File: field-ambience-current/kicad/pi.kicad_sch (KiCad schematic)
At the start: 9 parts, among them J4 SWD 1.27mm (SWCLK/GND/SWDIO), SW11 Reset 6mm SMD, SW12 BOOTSEL 6mm SMD (DNP for THT-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, U1 Raspberry_Pi_Pico2 (RP2350)

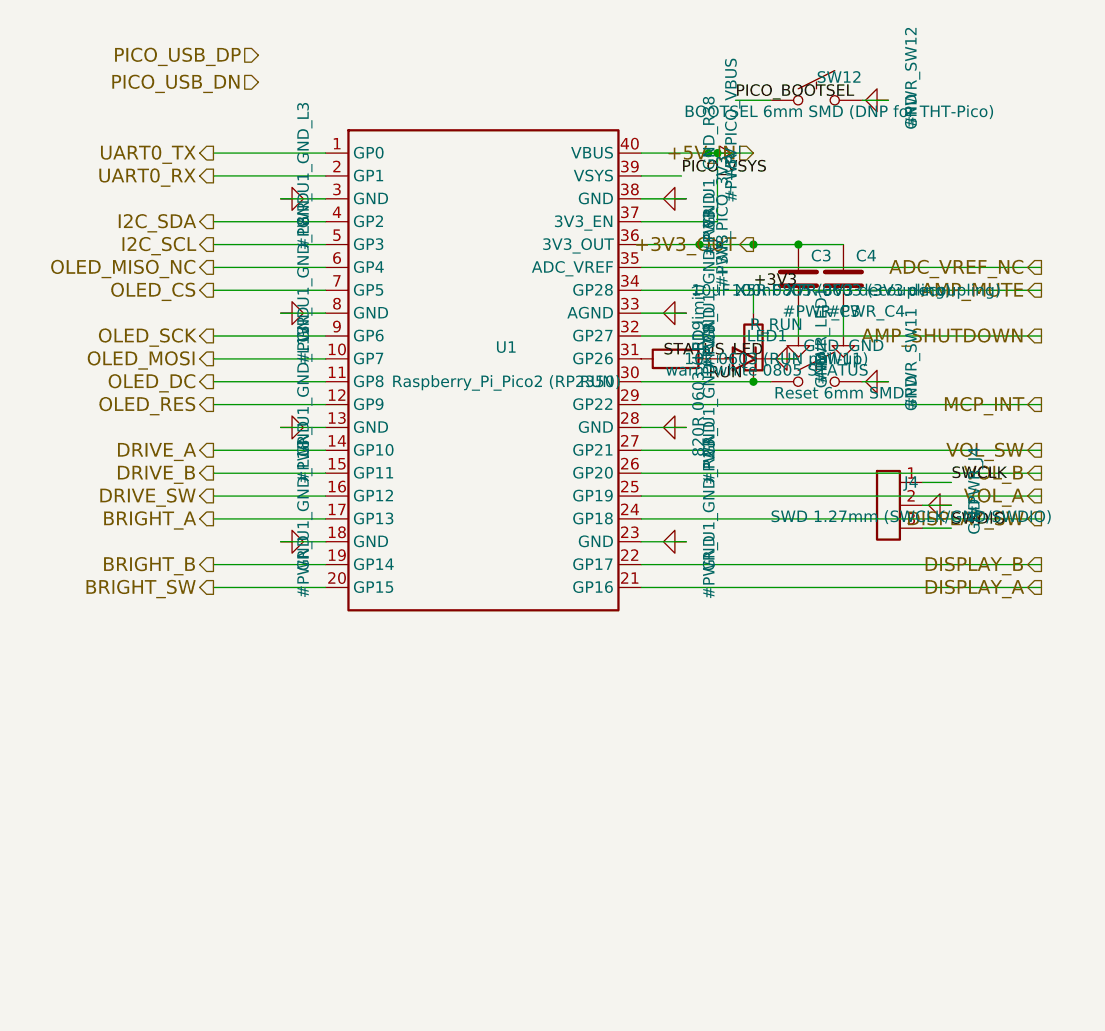
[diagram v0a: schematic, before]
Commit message: Add Sheet 7 (Pi Zero 2 W GPIO Header) per SPEC v0.6 §1/§8
J2 2x20 GPIO Header für Pi Zero 2 W:
- Pin 2, 4: +5V Power-Injection (von unserer PCB-Rail zum Pi)
- Pin 6, 9, 14, 20, 25, 30, 34, 39: GND (8x Pi GND-Pins)
- Pin 1, 17: NC (Pi 3V3 output ungenutzt — unsere 3V3 kommt vom Pico SMPS)

UART (115200) Pi ↔ Pico:
- Pin 10 (Pi GPIO15 RX) ← UART0_TX (von Pico GP0 direkt)
- Pin 8 (Pi GPIO14 TX) → R1 1k series → UART0_RX (zu Pico GP1, per SPEC v0.6 §5 BOM)

I²S Audio Pi → PCM5102A:
- Pin 12 (Pi GPIO18 PCM_CLK) → I2S_BCK
- Pin 35 (Pi GPIO19 PCM_FS) → I2S_LRCK
- Pin 40 (Pi GPIO21 PCM_DOUT) → I2S_DOUT

Alle 23 ungenutzten GPIOs (3, 5, 7, 11, 13, 15, 16, 18, 19, 21-24, 26-29,
31-33, 36-38) als NC-Labels mit informativen Namen markiert
(NC_GPIO2_SDA1, NC_GPIO10_MOSI, etc).

Root sheet: Pi-Sheet bei (330, 40) size (60, 130) mit 5 sheet-pins.
Pico-Sheet bekommt UART0_TX (output) + UART0_RX (input) auf linker Seite.
Label-bridges für UART (Pico↔Pi) und I2S (Pi→Audio).

Conn_02x20 generic lib_symbol generator hinzugefügt (alternating
odd/even Pin-Numbering, 2.54mm spacing).

Analyzer: 0 functional errors (3 VM-001 false positives unverändert).
19 warnings (von 24 gefallen, UART/I2S jetzt closed loop). 83 components
total (28 caps, 24 resistors, 16 switches, 6 connectors, 4 ICs, 2 diodes,
1 fuse, 1 ferrite, 1 LED).

J2 pin_nets verifiziert: alle Power-Pins korrekt, alle GND-Pins korrekt,
UART/I2S-Verbindungen passen zum SPEC §8.

**Damit ist die KiCad-Schematic-Eingabe für SPEC v0.6 komplett.**
Next Steps: ERC clean in KiCad GUI, PCB-Layout, DRC, BOM, JLC-Order.
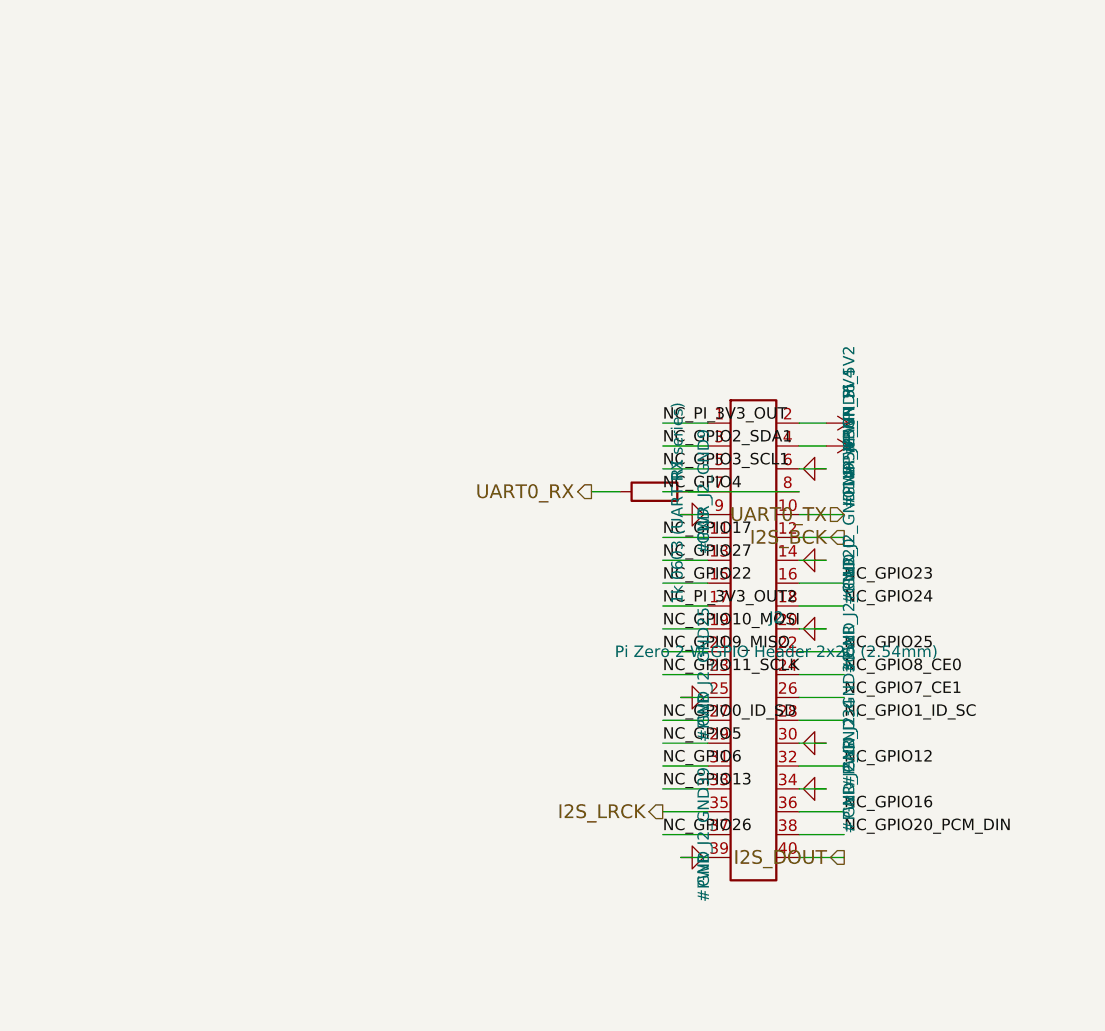
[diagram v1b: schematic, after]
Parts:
- removed C3: 10uF X5R 0805 (3V3 decoupling), Capacitor_SMD:C_0805_2012Metric, symbol Device:C
- removed C4: 100nF X7R 0603 (3V3 decoupling), Capacitor_SMD:C_0603_1608Metric, symbol Device:C
- removed J4: SWD 1.27mm (SWCLK/GND/SWDIO), Connector_PinHeader_1.27mm:PinHeader_1x03_P1.27mm_Vertical, symbol Connector:Conn_01x03
- removed LED1: warm white 0805 STATUS, LED_SMD:LED_0805_2012Metric, symbol Device:LED
- removed R19: 820R 0603 (LED limit), Resistor_SMD:R_0603_1608Metric, symbol Device:R
- removed R_RUN: 10k 0603 (RUN pull-up), Resistor_SMD:R_0603_1608Metric, symbol Device:R
- removed SW11: Reset 6mm SMD, Button_Switch_SMD:SW_SPST_TL3342, symbol Switch:SW_Push
- removed SW12: BOOTSEL 6mm SMD (DNP for THT-Pico), Button_Switch_SMD:SW_SPST_TL3342, symbol Switch:SW_Push
- removed U1: Raspberry_Pi_Pico2 (RP2350), MCU_Module:RPi_Pico_SMD_TH, symbol MCU:Pico2
- added J2: Pi Zero 2 W GPIO Header 2x20 (2.54mm), Connector_PinHeader_2.54mm:PinHeader_2x20_P2.54mm_Vertical, symbol Connector:Conn_02x20
- added R1: 1k 0603 (UART RX series), Resistor_SMD:R_0603_1608Metric, symbol Device:R
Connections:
- net +5V: now also J2.2 (Pin_2), J2.4 (Pin_4)
- net GND: now also J2.14 (Pin_14), J2.20 (Pin_20), J2.25 (Pin_25), J2.30 (Pin_30), J2.34 (Pin_34), J2.39 (Pin_39), J2.6 (Pin_6), J2.9 (Pin_9)
- net UART0_RX: now also R1.1
- net UART0_TX: now also J2.10 (Pin_10)
- new net I2S_BCK: J2.12 (Pin_12)
- new net I2S_DOUT: J2.40 (Pin_40)
- new net I2S_LRCK: J2.35 (Pin_35)
- new net NC_GPIO0_ID_SD: J2.27 (Pin_27)
- new net NC_GPIO10_MOSI: J2.19 (Pin_19)
- new net NC_GPIO11_SCLK: J2.23 (Pin_23)
- new net NC_GPIO12: J2.32 (Pin_32)
- new net NC_GPIO13: J2.33 (Pin_33)
- new net NC_GPIO16: J2.36 (Pin_36)
- new net NC_GPIO17: J2.11 (Pin_11)
- new net NC_GPIO1_ID_SC: J2.28 (Pin_28)
- new net NC_GPIO20_PCM_DIN: J2.38 (Pin_38)
- new net NC_GPIO22: J2.15 (Pin_15)
- new net NC_GPIO23: J2.16 (Pin_16)
- new net NC_GPIO24: J2.18 (Pin_18)
- new net NC_GPIO25: J2.22 (Pin_22)
- new net NC_GPIO26: J2.37 (Pin_37)
- new net NC_GPIO27: J2.13 (Pin_13)
- new net NC_GPIO2_SDA1: J2.3 (Pin_3)
- new net NC_GPIO3_SCL1: J2.5 (Pin_5)
- new net NC_GPIO4: J2.7 (Pin_7), J2.8 (Pin_8), R1.2
- new net NC_GPIO5: J2.29 (Pin_29)
- new net NC_GPIO6: J2.31 (Pin_31)
- new net NC_GPIO7_CE1: J2.26 (Pin_26)
- new net NC_GPIO8_CE0: J2.24 (Pin_24)
- new net NC_GPIO9_MISO: J2.21 (Pin_21)
- new net NC_PI_3V3_OUT: J2.1 (Pin_1)
- new net NC_PI_3V3_OUT2: J2.17 (Pin_17)
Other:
- title: Field Ambience PCB — Sheet 2: Pico 2 (RP2350) -> Field Ambience PCB — Sheet 7: Pi Zero 2 W GPIO Header

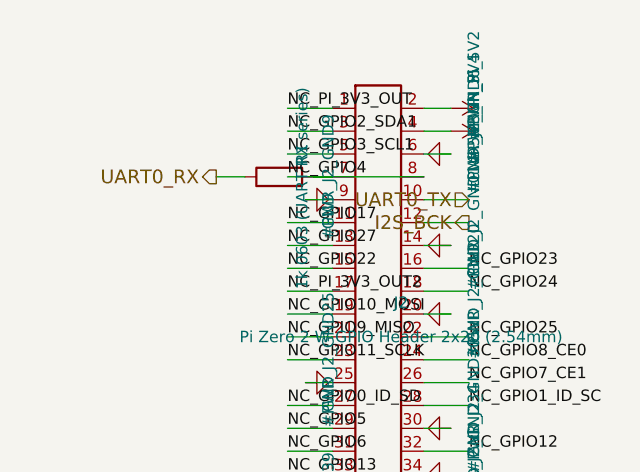
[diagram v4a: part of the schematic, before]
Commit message: v0.6.3-r2: PAM8403 SHDN/MUTE pull-downs + UART naming + TODO list
Addresses 2nd-iteration ChatGPT review findings (most that don't need
KiCad GUI). All TODO items documented in PCB_TODO.md.

B4: PAM8403H /SHDN and /MUTE hardware pull-downs
- R_MUTE_PD 10k from pin 5 (/MUTE) to GND
- R_SHDN_PD 10k from pin 12 (/SHDN) to GND
- Default state during Pico boot/reset = both LOW = Amp OFF + MUTED
- Pico firmware drives HIGH only after power-sequencing per SPEC §5
- Prevents undefined Amp state during boot transients (pop/click safety)

I7: UART net naming disambiguated
- Old: UART0_TX / UART0_RX (perspective-ambiguous)
- New:
  - PICO_TX_PI_RX (Pico GP0 → Pi GPIO15 pin 10)
  - PI_TX_PICO_RX (Pi GPIO14 pin 8 → R1 1k → Pico GP1)
- Changed in pico_sheet, pi_sheet, root_sheet (pins + labels)

N4: Titleblock revs synced
- audio.kicad_sch: v0.6.1 → v0.6.3
- power_tree.kicad_sch: v0.6 → v0.6.3
- Comments updated to reflect current state

N5: Stale comments cleanup
- power_tree_sheet: USB-C pin-number references updated to USB-C spec
- audio_sheet: PAM8403 references updated to PAM8403H + PDF reference
- BLOCKER-comment in audio sheet replaced with "boot-safe pull-downs added"

New PCB_TODO.md tracks remaining items for PCB-layout readiness:
- BLOCKER (4): need KiCad GUI — footprint verification, ERC report
- IMPORTANT (7): power budget recalc, mech coords, BOM split, etc.
- NICE-TO-HAVE (5): XSMT via GPIO, I²S series R, etc.

Analyzer status: 0 functional errors (same 3 VM-001 false positives),
19 warnings, 87 components (was 85, +2 for pull-downs), 117 nets.

Verified via analyzer pin_nets:
- R_MUTE_PD: pin1=AMP_MUTE, pin2=GND ✓
- R_SHDN_PD: pin1=AMP_SHUTDOWN, pin2=GND ✓
- U1 Pin 1 (GP0) = PICO_TX_PI_RX ✓
- U1 Pin 2 (GP1) = PI_TX_PICO_RX ✓
- U4 Pin 5 (MUTE) = AMP_MUTE ✓
- U4 Pin 12 (SHDN) = AMP_SHUTDOWN ✓

Note on reviewer's USB-C claim: Reviewer indicated USB-C symbol still
has wrong pinout in PR. Verified via GitHub API that PR HEAD (commit
5ca0bcb) has the correct mapping (VB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
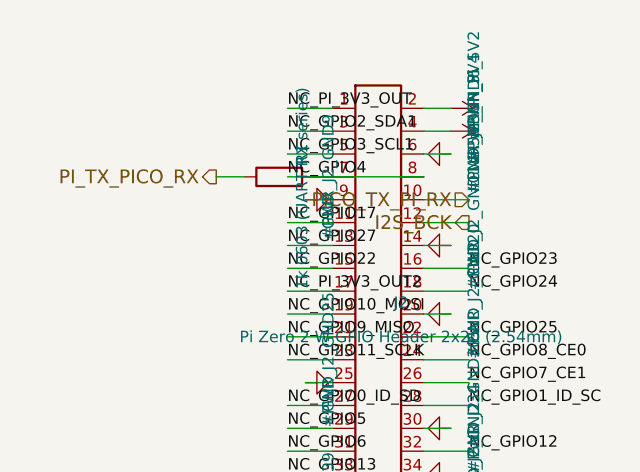
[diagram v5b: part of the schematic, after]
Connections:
- net UART0_RX renamed PI_TX_PICO_RX
- net UART0_TX renamed PICO_TX_PI_RX
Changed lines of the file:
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@@
     (effects (font (size 1.524 1.524)) (justify right))
 )
-  (hierarchical_label "UART0_RX" (shape output) (at 112 113.49000000000001 0)
+  (hierarchical_label "PI_TX_PICO_RX" (shape output) (at 112 113.49000000000001 0)
     (effects (font (size 1.524 1.524)) (justify right))
 )
-  (hierarchical_label "UART0_TX" (shape input) (at 140.08 116.03 180)
+  (hierarchical_label "PICO_TX_PI_RX" (shape input) (at 140.08 116.03 180)
     (effects (font (size 1.524 1.524)) (justify right))
 )

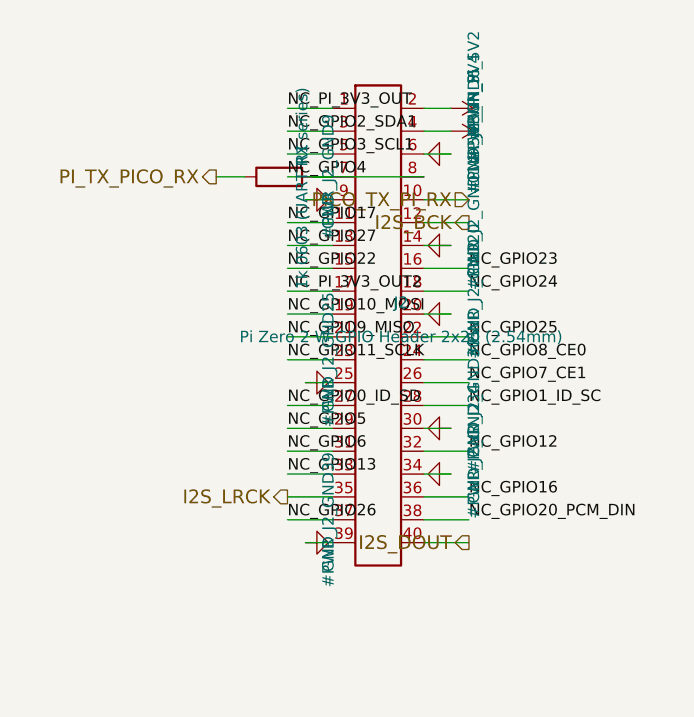
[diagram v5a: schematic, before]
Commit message: v0.6.3-r3: Important + Nice-to-Have items (all non-KiCad-GUI doable)
Addresses I1-I6 + N2 + N3 from PCB_TODO.md. Only schematic-level
hardware change is N2 (I²S series resistors); rest are doc updates.

N2 — I²S Series-Resistoren am Pi-Header (HARDWARE):
- R_BCK 33Ω 0603 between Pi pin 12 (GPIO18 PCM_CLK) and I2S_BCK hier
- R_LRCK 33Ω 0603 between Pi pin 35 (GPIO19 PCM_FS) and I2S_LRCK hier
- R_DOUT 33Ω 0603 between Pi pin 40 (GPIO21 PCM_DOUT) and I2S_DOUT hier
- Dämpft Overshoot/Reflexionen über lange I²S-Strecke (~100mm Layer-Hop)
- LCSC C23138 (RC0603FR-0733RL)

I1 — Power-Budget realistisch (Doc):
- Was 1.4 A peak in v0.6 → realistisch 2.48 A peak im Worst-Case
- PAM8403 @ 4Ω 6W out = ~1.4 A (statt 350 mA wie in v0.6)
- Empfehlung Variante (a): Firmware Volume-Clamp auf max 50%

I2 — USB-C Power-Negotiation (Doc):
- 5.1k CC = "Sink", garantiert kein 3A
- Decision: Variante A (Firmware-Volume-Clamp) für Prototyp
- Future: USB-PD-Sink-Controller (TPS25750 oder CYPD3177) für Produkt

I3 — Inrush-Strategie (Doc):
- C_BULK MPN-Spec auf Low-ESR Polymer (Nichicon PCV1A102MCL1GS)
- NTC-Inrush-Limiter (Ametherm CL-130) als DNP-Option für Production

I4 — 4-Layer-Stack-Up überdacht (Doc):
- Alt: Signal/GND/+3V3/Signal
- Neu: Signal/GND/+5V/Signal (+5V ist die Hochstrom-Schiene)
- GND-Plane darf NICHT unter USB-C, I²S, Audio-Out gesplittet werden

I5 — Mechanical Coordinates (neue Datei mechanical_coordinates.md):
- Außen 333×143.3×40, PCB 320×130
- X/Y-Tabellen für Encoder, Cells, Modifier, Speaker, OLED, Mounting-Holes
- Component-Height-Zones je Gehäuse-Bereich
- TODO-Liste was noch im CAD final festgelegt werden muss

I6 — BOM-Split sauber in SPEC:
- Section A: JLCPCB Full-PCBA (~70 SKUs) — alle Passives, Power-ICs, Connectors
- Section B: Manuell (~15 Items) — Pico/Pi/OLED-Module, Hot-Swap-Sockets, Speaker, Stabilizer
- Section C: TBD — Custom Caps, Schraubdome, USB-Netzteil

N3 — ERC-Report-Workflow in SPEC dokumentiert:
- kicad-cli sch erc Command-Beispiel
- Report-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
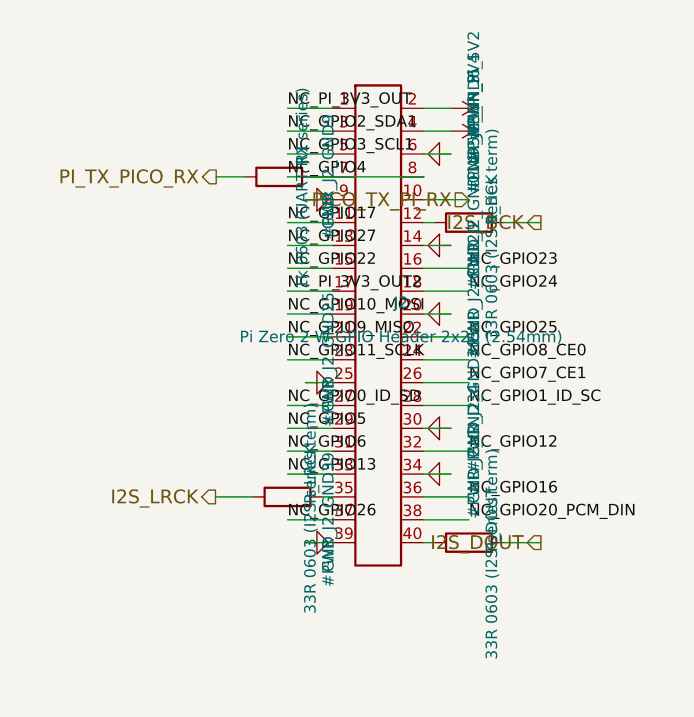
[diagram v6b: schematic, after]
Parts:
- added R_BCK, R_DOUT, R_LRCK: 33R 0603 (I2S series term), Resistor_SMD:R_0603_1608Metric, symbol Device:R
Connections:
- net I2S_BCK: now also R_BCK.2; no longer J2.12 (Pin_12)
- net I2S_DOUT: now also R_DOUT.2; no longer J2.40 (Pin_40)
- net I2S_LRCK: now also R_LRCK.1; no longer J2.35 (Pin_35)
- new net: J2.12 (Pin_12), R_BCK.1
- new net: J2.40 (Pin_40), R_DOUT.1
- new net: J2.35 (Pin_35), R_LRCK.2
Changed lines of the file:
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@@
       (project "field_ambience"
         (path "/85f2b7f7-647f-4a96-a4c2-866fed7d38ad" (reference "#PWR_J2_GND39") (unit 1)))))
+  (symbol (lib_id "Device:R") (at 140.08 118.57000000000001 90) (unit 1)
+    (in_bom yes) (on_board yes) (dnp no)
+      (property "Reference" "R_BCK" (at 142.62 116.03 0)
+        (effects (font (size 1.27 1.27))))
+      (property "Value" "33R 0603 (I2S series term)" (at 142.62 119.84 0)
+        (effects (font (size 1.27 1.27))))
+      (property "Footprint" "Resistor_SMD:R_0603_1608Metric" (at 140.08 118.57000000000001 0)
+        (effects (font (size 1.27 1.27)) hide))
+      (property "Datasheet" "~" (at 140.08 118.57000000000001 0)
+        (effects (font (size 1.27 1.27)) hide))
+      (property "MPN" "RC0603FR-0733RL" (at 142.62 122.38000000000001 0)
+        (effects (font (size 1.27 1.27)) hide))
+      (property "LCSC" "C23138" (at 142.62 123.65 0)
+        (effects (font (size 1.27 1.27)) hide))
+    (instances
+      (project "field_ambience"
+        (path "/85f2b7f7-647f-4a96-a4c2-866fed7d38ad" (reference "R_BCK") (unit 1)))))
+  (symbol (lib_id "Device:R") (at 119.92 149.05 90) (unit 1)
+    (in_bom yes) (on_board yes) (dnp no)
+      (property "Reference" "R_LRCK" (at 122.46000000000001 146.51000000000002 0)
+        (effects (font (size 1.27 1.27))))
+      (property "Value" "33R 0603 (I2S series term)" (at 122.46000000000001 150.32000000000002 0)
+        (effects (font (size 1.27 1.27))))
+      (property "Footprint" "Resistor_SMD:R_0603_1608Metric" (at 119.92 149.05 0)
+        (effects (font (size 1.27 1.27)) hide))
+      (property "Datasheet" "~" (at 119.92 149.05 0)
+        (effects (font (size 1.27 1.27)) hide))
+      (property "MPN" "RC0603FR-0733RL" (at 122.46000000000001 152.86 0)
+        (effects (font (size 1.27 1.27)) hide))
+      (property "LCSC" "C23138" (at 122.46000000000001 154.13000000000002 0)
+        (effects (font (size 1.27 1.27)) hide))
+    (instances
+      (project "field_ambience"
+        (path "/85f2b7f7-647f-4a96-a4c2-866fed7d38ad" (reference "R_LRCK") (unit 1)))))
+  (symbol (lib_id "Device:R") (at 140.08 154.13 90) (unit 1)
+    (in_bom yes) (on_board yes) (dnp no)
+      (property "Reference" "R_DOUT" (at 142.62 151.59 0)
+        (effects (font (size 1.27 1.27))))
+      (property "Value" "33R 0603 (I2S series term)" (at 142.62 155.4 0)
+        (effects (font (size 1.27 1.27))))
+      (property "Footprint" "Resistor_SMD:R_0603_1608Metric" (at 140.08 154.13 0)
+        (effects (font (size 1.27 1.27)) hide))
+      (property "Datasheet" "~" (at 140.08 154.13 0)
+        (effects (font (size 1.27 1.27)) hide))
+      (property "MPN" "RC0603FR-0733RL" (at 142.62 157.94 0)
+        (effects (font (size 1.27 1.27)) hide))
+      (property "LCSC" "C23138" (at 142.62 159.21 0)
+        (effects (font (size 1.27 1.27)) hide))
+    (instances
+      (project "field_ambience"
+        (path "/85f2b7f7-647f-4a96-a4c2-866fed7d38ad" (reference "R_DOUT") (unit 1)))))
   (symbol (lib_id "Device:R") (at 119 113.49000000000001 90) (unit 1)
     (in_bom yes) (on_board yes) (dnp no)
@@
     (stroke (width 0) (type default))
 )
-  (wire (pts (xy 135.08 118.57000000000001) (xy 140.08 118.57000000000001))
-    (stroke (width 0) (type default))
-)
-  (wire (pts (xy 124.92 149.05) (xy 119.92 149.05))
-    (stroke (width 0) (type default))
-)
-  (wire (pts (xy 135.08 154.13) (xy 140.08 154.13))
+  (wire (pts (xy 135.08 118.57000000000001) (xy 136.27 118.57000000000001))
+    (stroke (width 0) (type default))
+)
+  (wire (pts (xy 143.89000000000001 118.57000000000001) (xy 148.08 118.57000000000001))
+    (stroke (width 0) (type default))
+)
+  (wire (pts (xy 124.92 149.05) (xy 123.73 149.05))
+    (stroke (width 0) (type default))
+)
+  (wire (pts (xy 116.11 149.05) (xy 111.92 149.05))
+    (stroke (width 0) (type default))
+)
+  (wire (pts (xy 135.08 154.13) (xy 136.27 154.13))
+    (stroke (width 0) (type default))
+)
+  (wire (pts (xy 143.89000000000001 154.13) (xy 148.08 154.13))
     (stroke (width 0) (type default))
 )
@@
     (effects (font (size 1.27 1.27)) (justify left bottom))
 )
-  (hierarchical_label "I2S_BCK" (shape output) (at 140.08 118.57000000000001 180)
+  (hierarchical_label "I2S_BCK" (shape output) (at 148.08 118.57000000000001 180)
     (effects (font (size 1.524 1.524)) (justify right))
 )
-  (hierarchical_label "I2S_LRCK" (shape output) (at 119.92 149.05 0)
+  (hierarchical_label "I2S_LRCK" (shape output) (at 111.92 149.05 0)
     (effects (font (size 1.524 1.524)) (justify right))
 )
-  (hierarchical_label "I2S_DOUT" (shape output) (at 140.08 154.13 180)
+  (hierarchical_label "I2S_DOUT" (shape output) (at 148.08 154.13 180)
     (effects (font (size 1.524 1.524)) (justify right))
 )
